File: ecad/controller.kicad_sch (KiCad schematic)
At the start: 53 parts, among them J1 PPTC141LGBN-RC, J2 PH1RB-14-UA, J3 Conn_01x06_Socket, J4 Conn_01x06_Socket, J5 Conn_01x06_Socket, J6 PPPC101LFBN-RC, J7 PPTC161LFBN-RC, SW1 PEC11R-4220F-S0024, U1 TMC5041, U2 TMC5041

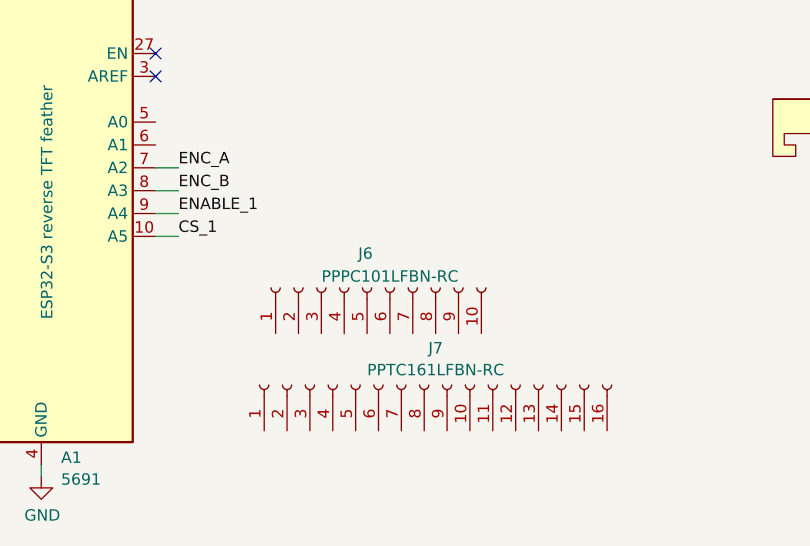
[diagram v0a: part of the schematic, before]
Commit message: change BOM to use 12-pin female header
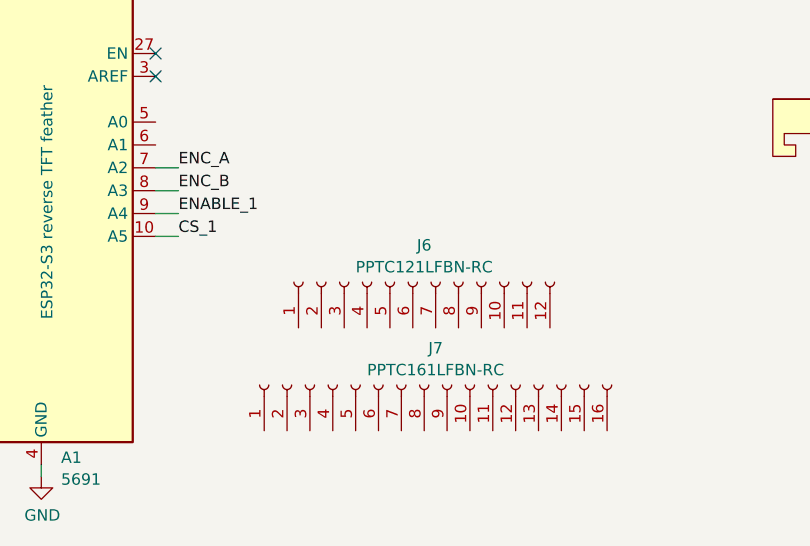
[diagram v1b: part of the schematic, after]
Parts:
- removed J6: PPPC101LFBN-RC, symbol Connector:Conn_01x10_Socket
- added J6: PPTC121LFBN-RC, symbol Connector:Conn_01x12_Socket
- J3, J4, J5: now left out of the parts list
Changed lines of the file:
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@@
+	)
+	(symbol
+		(lib_id "Connector:Conn_01x12_Socket")
+		(at 116.84 168.91 90)
+		(unit 1)
+		(exclude_from_sim no)
+		(in_bom yes)
+		(on_board yes)
+		(dnp no)
+		(property "Reference" "J6"
+			(at 118.11 164.8163 90)
+			(effects
+				(font
+					(size 1.27 1.27)
+				)
+			)
+		)
+		(property "Value" "PPTC121LFBN-RC"
+			(at 118.11 167.2406 90)
+			(effects
+				(font
+					(size 1.27 1.27)
+				)
+			)
+		)
+		(property "Footprint" ""
+			(at 116.84 168.91 0)
+			(effects
+				(font
+					(size 1.27 1.27)
+				)
+				(hide yes)
+			)
+		)
+		(property "Datasheet" "https://www.digikey.com/en/products/detail/sullins-connector-solutions/PPTC121LFBN-RC/807231"
+			(at 116.84 168.91 0)
+			(effects
+				(font
+					(size 1.27 1.27)
+				)
+				(hide yes)
+			)
+		)
+		(property "Description" "12-pin female header"
+			(at 116.84 168.91 0)
+			(effects
+				(font
+					(size 1.27 1.27)
+				)
+				(hide yes)
+			)
+		)
+		(pin "1"
+		)
+		(pin "2"
+		)
+		(pin "4"
+		)
+		(pin "5"
+		)
+		(pin "6"
+		)
+		(pin "7"
+		)
+		(pin "8"
+		)
+		(pin "9"
+		)
+		(pin "10"
+		)
+		(pin "11"
+		)
+		(pin "12"
+		)
+		(pin "3"
+		)
+		(instances
+			(project ""
+				(path "/c5d11359-d95e-4186-8c82-8e7791451f5a"
+					(reference "J6")
+					(unit 1)
+				)
+			)
+		)
 	)
 	(symbol
@@
 				(path "/c5d11359-d95e-4186-8c82-8e7791451f5a"
 					(reference "R17")
-					(unit 1)
-				)
-			)
-		)
-	)
-	(symbol
-		(lib_id "Connector:Conn_01x10_Socket")
-		(at 111.76 169.545 90)
-		(unit 1)
-		(exclude_from_sim no)
-		(in_bom yes)
-		(on_board yes)
-		(dnp no)
-		(property "Reference" "J6"
-			(at 112.395 165.735 90)
-			(effects
-				(font
-					(size 1.27 1.27)
-				)
-				(justify left)
-			)
-		)
-		(property "Value" "PPPC101LFBN-RC"
-			(at 121.92 168.275 90)
-			(effects
-				(font
-					(size 1.27 1.27)
-				)
-				(justify left)
-			)
-		)
-		(property "Footprint" ""
-			(at 111.76 169.545 0)
-			(effects
-				(font
-					(size 1.27 1.27)
-				)
-				(hide yes)
-			)
-		)
-		(property "Datasheet" "https://www.digikey.com/en/products/detail/sullins-connector-solutions/PPPC101LFBN-RC/810182?s=N4IgTCBcDaIM4HYAMAWAzCAugXyA"
-			(at 111.76 169.545 0)
-			(effects
-				(font
-					(size 1.27 1.27)
-				)
-				(hide yes)
-			)
-		)
-		(property "Description" "10-pin female header"
-			(at 111.76 169.545 0)
-			(effects
-				(font
-					(size 1.27 1.27)
-				)
-				(hide yes)
-			)
-		)
-		(pin "1"
-		)
-		(pin "10"
-		)
-		(pin "8"
-		)
-		(pin "9"
-		)
-		(pin "4"
-		)
-		(pin "2"
-		)
-		(pin "6"
-		)
-		(pin "7"
-		)
-		(pin "3"
-		)
-		(pin "5"
-		)
-		(instances
-			(project ""
-				(path "/c5d11359-d95e-4186-8c82-8e7791451f5a"
-					(reference "J6")
 					(unit 1)
 				)
@@
 		(unit 1)
 		(exclude_from_sim no)
-		(in_bom yes)
+		(in_bom no)
 		(on_board yes)
 		(dnp no)
@@
 		(unit 1)
 		(exclude_from_sim no)
-		(in_bom yes)
+		(in_bom no)
 		(on_board yes)
 		(dnp no)
@@
 		(unit 1)
 		(exclude_from_sim no)
-		(in_bom yes)
-		(on_board yes)
-		(dnp no)
+		(in_bom no)
+		(on_board yes)
+		(dnp no)
